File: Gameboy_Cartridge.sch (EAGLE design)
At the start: 10 parts, among them IC1 AT49F040J

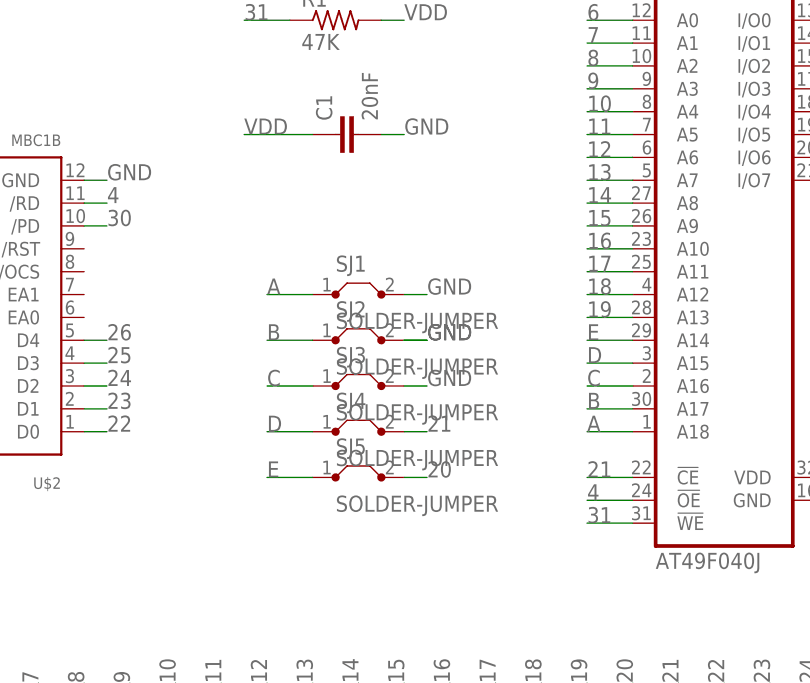
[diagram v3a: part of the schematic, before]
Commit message: Fix the connections on the solder jumper
No ERC errors
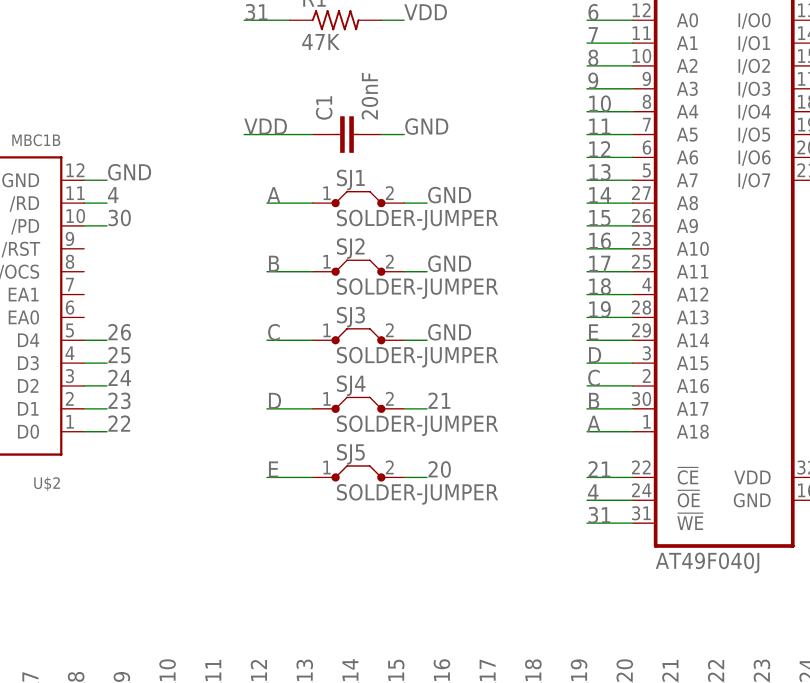
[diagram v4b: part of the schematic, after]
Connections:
- net 20: now also SJ5.2
- net 21: now also SJ4.2
- net B: no longer SJ3.1, SJ4.1
- net C: now also SJ3.1
- net D: now also SJ4.1
- net E: now also SJ5.1
- net GND: no longer SJ4.2
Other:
- moved on the sheet: SJ1, SJ2, SJ3, SJ4
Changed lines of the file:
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@@
 <attribute name="VALUE" x="60.579" y="118.364" size="1.778" layer="96" rot="R90"/>
 </instance>
-<instance part="SJ1" gate="G$1" x="58.42" y="99.06" smashed="yes">
-<attribute name="NAME" x="55.88" y="101.6" size="1.778" layer="95"/>
-<attribute name="VALUE" x="55.88" y="95.25" size="1.778" layer="96"/>
+<instance part="SJ1" gate="G$1" x="58.42" y="109.22" smashed="yes">
+<attribute name="NAME" x="55.88" y="111.125" size="1.778" layer="95"/>
+<attribute name="VALUE" x="55.88" y="106.68" size="1.778" layer="96"/>
 </instance>
-<instance part="SJ2" gate="G$1" x="58.42" y="93.98" smashed="yes">
-<attribute name="NAME" x="55.88" y="96.52" size="1.778" layer="95"/>
-<attribute name="VALUE" x="55.88" y="90.17" size="1.778" layer="96"/>
+<instance part="SJ2" gate="G$1" x="58.42" y="101.6" smashed="yes">
+<attribute name="NAME" x="55.88" y="103.505" size="1.778" layer="95"/>
+<attribute name="VALUE" x="55.88" y="99.06" size="1.778" layer="96"/>
 </instance>
-<instance part="SJ3" gate="G$1" x="58.42" y="88.9" smashed="yes">
-<attribute name="NAME" x="55.88" y="91.44" size="1.778" layer="95"/>
-<attribute name="VALUE" x="55.88" y="85.09" size="1.778" layer="96"/>
+<instance part="SJ3" gate="G$1" x="58.42" y="93.98" smashed="yes">
+<attribute name="NAME" x="55.88" y="95.885" size="1.778" layer="95"/>
+<attribute name="VALUE" x="55.88" y="91.44" size="1.778" layer="96"/>
 </instance>
-<instance part="SJ4" gate="G$1" x="58.42" y="83.82" smashed="yes">
-<attribute name="NAME" x="55.88" y="86.36" size="1.778" layer="95"/>
-<attribute name="VALUE" x="55.88" y="80.01" size="1.778" layer="96"/>
+<instance part="SJ4" gate="G$1" x="58.42" y="86.36" smashed="yes">
+<attribute name="NAME" x="55.88" y="88.265" size="1.778" layer="95"/>
+<attribute name="VALUE" x="55.88" y="83.82" size="1.778" layer="96"/>
 </instance>
 <instance part="SJ5" gate="G$1" x="58.42" y="78.74" smashed="yes">
-<attribute name="NAME" x="55.88" y="81.28" size="1.778" layer="95"/>
-<attribute name="VALUE" x="55.88" y="74.93" size="1.778" layer="96"/>
+<attribute name="NAME" x="55.88" y="80.645" size="1.778" layer="95"/>
+<attribute name="VALUE" x="55.88" y="76.2" size="1.778" layer="96"/>
 </instance>
 </instances>
@@
 <wire x1="0" y1="91.44" x2="5.08" y2="91.44" width="0.1524" layer="91"/>
 <label x="0" y="91.44" size="1.778" layer="95"/>
-<label x="66.04" y="83.82" size="1.778" layer="95"/>
 </segment>
 <segment>
@@
 <label x="83.82" y="78.74" size="1.778" layer="95"/>
 </segment>
+<segment>
+<pinref part="SJ4" gate="G$1" pin="2"/>
+<wire x1="63.5" y1="86.36" x2="66.04" y2="86.36" width="0.1524" layer="91"/>
+<label x="66.04" y="86.36" size="1.778" layer="95"/>
+</segment>
 </net>
 <net name="20" class="0">
@@
 <wire x1="5.08" y1="93.98" x2="0" y2="93.98" width="0.1524" layer="91"/>
 <label x="0" y="93.98" size="1.778" layer="95"/>
-<label x="66.04" y="78.74" size="1.778" layer="95"/>
 </segment>
 <segment>
@@
 <label x="88.9" y="55.88" size="1.778" layer="95" rot="R90"/>
 </segment>
+<segment>
+<pinref part="SJ5" gate="G$1" pin="2"/>
+<wire x1="63.5" y1="78.74" x2="66.04" y2="78.74" width="0.1524" layer="91"/>
+<label x="66.04" y="78.74" size="1.778" layer="95"/>
+</segment>
 </net>
 <net name="19" class="0">
@@
 <wire x1="5.08" y1="99.06" x2="0" y2="99.06" width="0.1524" layer="91"/>
 <label x="0" y="99.06" size="1.778" layer="95"/>
+</segment>
+<segment>
+<pinref part="SJ5" gate="G$1" pin="1"/>
+<wire x1="53.34" y1="78.74" x2="48.26" y2="78.74" width="0.1524" layer="91"/>
 <label x="48.26" y="78.74" size="1.778" layer="95"/>
 </segment>
@@
 <wire x1="0" y1="101.6" x2="5.08" y2="101.6" width="0.1524" layer="91"/>
 <label x="0" y="101.6" size="1.778" layer="95"/>
-<label x="48.26" y="83.82" size="1.778" layer="95"/>
+</segment>
+<segment>
+<pinref part="SJ4" gate="G$1" pin="1"/>
+<wire x1="53.34" y1="86.36" x2="48.26" y2="86.36" width="0.1524" layer="91"/>
+<label x="48.26" y="86.36" size="1.778" layer="95"/>
 </segment>
 </net>
@@
 <wire x1="5.08" y1="104.14" x2="0" y2="104.14" width="0.1524" layer="91"/>
 <label x="0" y="104.14" size="1.778" layer="95"/>
-<label x="48.26" y="88.9" size="1.778" layer="95"/>
+</segment>
+<segment>
+<pinref part="SJ3" gate="G$1" pin="1"/>
+<wire x1="53.34" y1="93.98" x2="48.26" y2="93.98" width="0.1524" layer="91"/>
+<label x="48.26" y="93.98" size="1.778" layer="95"/>
 </segment>
 </net>
@@
 <wire x1="60.96" y1="116.84" x2="63.5" y2="116.84" width="0.1524" layer="91"/>
 <label x="63.5" y="116.84" size="1.778" layer="95"/>
-<label x="66.04" y="99.06" size="1.778" layer="95"/>
+</segment>
+<segment>
+<pinref part="SJ2" gate="G$1" pin="2"/>
+<wire x1="63.5" y1="101.6" x2="66.04" y2="101.6" width="0.1524" layer="91"/>
+<label x="66.04" y="101.6" size="1.778" layer="95"/>
+</segment>
+<segment>
+<pinref part="SJ1" gate="G$1" pin="2"/>
+<wire x1="63.5" y1="109.22" x2="66.04" y2="109.22" width="0.1524" layer="91"/>
+<label x="66.04" y="109.22" size="1.778" layer="95"/>
+</segment>
+<segment>
+<pinref part="SJ3" gate="G$1" pin="2"/>
+<wire x1="63.5" y1="93.98" x2="66.04" y2="93.98" width="0.1524" layer="91"/>
 <label x="66.04" y="93.98" size="1.778" layer="95"/>
-<label x="66.04" y="93.98" size="1.778" layer="95"/>
-<label x="66.04" y="88.9" size="1.778" layer="95"/>
-</segment>
-<segment>
-<wire x1="63.5" y1="99.06" x2="66.04" y2="99.06" width="0.1524" layer="91"/>
-<pinref part="SJ1" gate="G$1" pin="2"/>
-</segment>
-<segment>
-<wire x1="63.5" y1="93.98" x2="66.04" y2="93.98" width="0.1524" layer="91"/>
-<pinref part="SJ2" gate="G$1" pin="2"/>
-<wire x1="63.5" y1="93.98" x2="66.04" y2="93.98" width="0.1524" layer="91"/>
-</segment>
-<segment>
-<wire x1="63.5" y1="88.9" x2="66.04" y2="88.9" width="0.1524" layer="91"/>
-<pinref part="SJ3" gate="G$1" pin="2"/>
-</segment>
-<segment>
-<wire x1="63.5" y1="83.82" x2="66.04" y2="83.82" width="0.1524" layer="91"/>
-<pinref part="SJ4" gate="G$1" pin="2"/>
-</segment>
-<segment>
-<wire x1="63.5" y1="78.74" x2="66.04" y2="78.74" width="0.1524" layer="91"/>
 </segment>
 </net>
@@
 <net name="31" class="0">
 <segment>
-<pinref part="U$1" gate="G$1" pin="VIN"/>
-<wire x1="144.78" y1="53.34" x2="144.78" y2="55.88" width="0.1524" layer="91"/>
-</segment>
-<segment>
 <pinref part="IC1" gate="G$1" pin="!WE"/>
 <wire x1="88.9" y1="73.66" x2="83.82" y2="73.66" width="0.1524" layer="91"/>
 <label x="83.82" y="73.66" size="1.778" layer="95"/>
-<label x="144.78" y="55.88" size="1.778" layer="95" rot="R90"/>
 </segment>
 <segment>
@@
 <label x="45.72" y="129.54" size="1.778" layer="95"/>
 </segment>
+<segment>
+<pinref part="U$1" gate="G$1" pin="VIN"/>
+<wire x1="144.78" y1="53.34" x2="144.78" y2="55.88" width="0.1524" layer="91"/>
+<label x="144.78" y="55.88" size="1.778" layer="95" rot="R90"/>
+</segment>
 </net>
 <net name="B" class="0">
@@
 <wire x1="0" y1="106.68" x2="5.08" y2="106.68" width="0.1524" layer="91"/>
 <label x="0" y="106.68" size="1.778" layer="95"/>
-<label x="48.26" y="93.98" size="1.778" layer="95"/>
-</segment>
-<segment>
-<wire x1="48.26" y1="93.98" x2="53.34" y2="93.98" width="0.1524" layer="91"/>
+</segment>
+<segment>
 <pinref part="SJ2" gate="G$1" pin="1"/>
-</segment>
-<segment>
-<wire x1="48.26" y1="88.9" x2="53.34" y2="88.9" width="0.1524" layer="91"/>
-<pinref part="SJ3" gate="G$1" pin="1"/>
-</segment>
-<segment>
-<wire x1="48.26" y1="83.82" x2="53.34" y2="83.82" width="0.1524" layer="91"/>
-<pinref part="SJ4" gate="G$1" pin="1"/>
-</segment>
-<segment>
-<wire x1="48.26" y1="78.74" x2="53.34" y2="78.74" width="0.1524" layer="91"/>
+<wire x1="53.34" y1="101.6" x2="48.26" y2="101.6" width="0.1524" layer="91"/>
+<label x="48.26" y="101.6" size="1.778" layer="95"/>
 </segment>
 </net>
@@
 <wire x1="5.08" y1="109.22" x2="0" y2="109.22" width="0.1524" layer="91"/>
 <label x="0" y="109.22" size="1.778" layer="95"/>
-<label x="48.26" y="99.06" size="1.778" layer="95"/>
-</segment>
-<segment>
-<wire x1="53.34" y1="99.06" x2="48.26" y2="99.06" width="0.1524" layer="91"/>
+</segment>
+<segment>
 <pinref part="SJ1" gate="G$1" pin="1"/>
-</segment>
-</net>
+<wire x1="53.34" y1="109.22" x2="48.26" y2="109.22" width="0.1524" layer="91"/>
+<label x="48.26" y="109.22" size="1.778" layer="95"/>
+</segment>
+</net>
